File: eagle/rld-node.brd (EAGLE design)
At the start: 160 x 100 mm, 11 parts

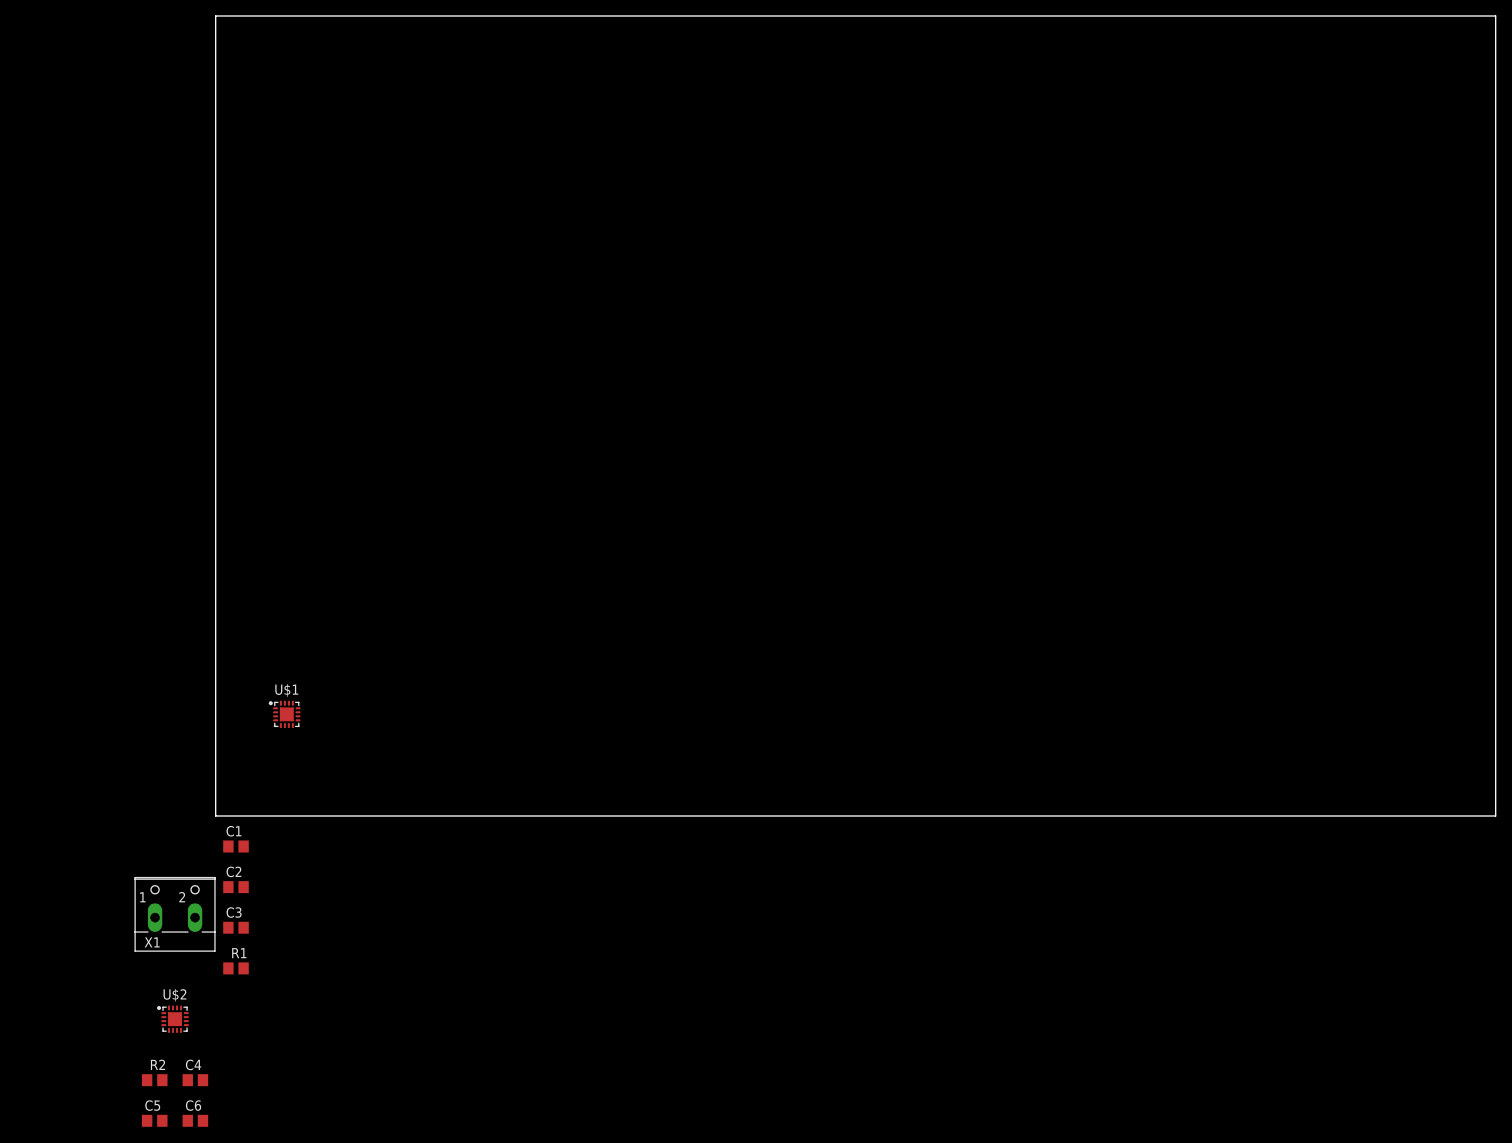
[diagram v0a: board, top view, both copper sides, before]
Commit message: Added synched layout
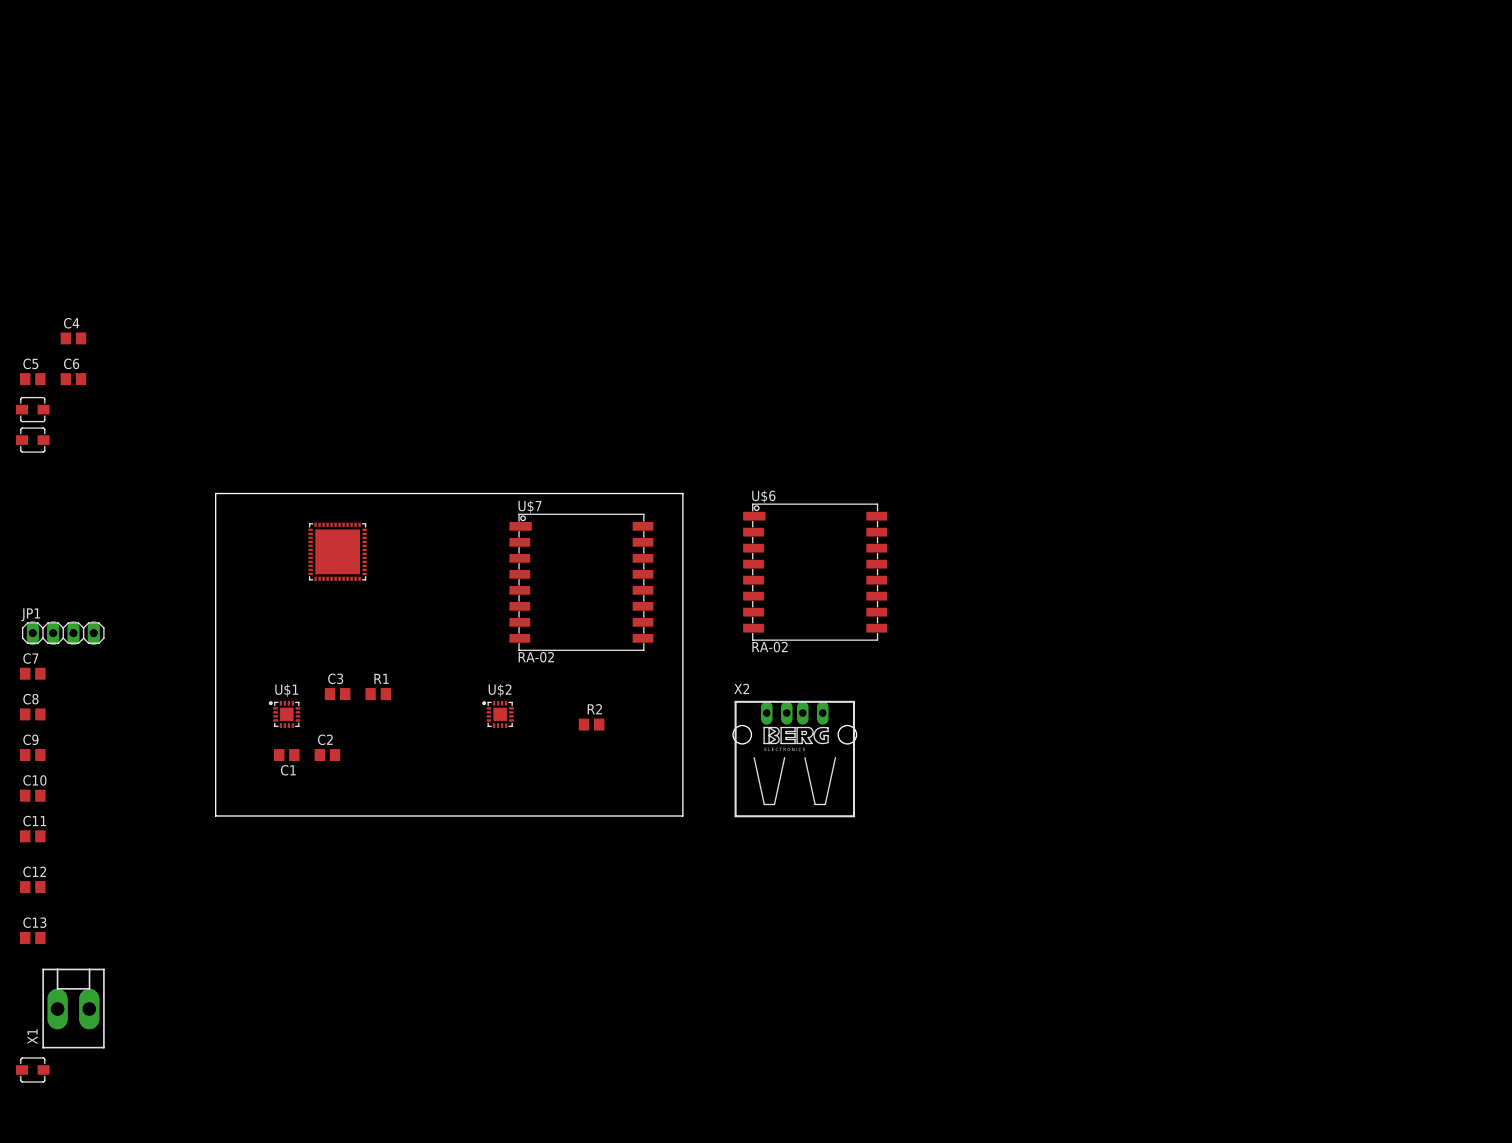
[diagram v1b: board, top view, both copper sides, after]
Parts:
- added C10, C7, C8: 100nF, rcl:C0805
- added C11: 4.7uF, rcl:C0805
- added C12: 10nF, rcl:C0805
- added C13: 1uF, rcl:C0805
- added C9: 4.7 uF, rcl:C0805
- added JP1: (no value), pinhead:1X04
- added U$3, U$4, U$8: IHLP-1212, inductor-vishay:1212BZ
- added U$5: STM32-F042X4/6-48, st-microelectronics:UFQFPN48-7X7
- added U$6, U$7: RA-02, ai-thinker:RA-01/RA-02
- added X2: (no value), con-berg:PN87520
- X1: device con-wago-500:W237-102 -> con-molex:KK-156-2
- moved C4 94.0 mm to (-17.8, 59.7)
- moved C5 94.0 mm to (-22.9, 54.6)
- moved C6 94.0 mm to (-17.8, 54.6)
- moved R2 70.4 mm to (47.0, 11.4)
- moved U$2 55.7 mm to (35.6, 12.7)
- moved R1 38.6 mm to (20.3, 15.2)
- moved C3 31.9 mm to (15.2, 15.2)
- moved C2 20.1 mm to (14.0, 7.62)
- moved X1 18.0 mm to (-17.8, -24.1)
- moved C1 13.1 mm to (8.89, 7.62), turned to 180 degrees
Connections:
- new net N$5: U$1.1, U$1.2, U$1.3, U$3.1
- new net N$6: U$2.1, U$2.2, U$2.3, U$4.1
- new net SPI1_MISO: U$5.16
- new net SPI1_MOSI: U$5.17
- new net SPI1_SCK: U$5.15
- new net SPI2_MISO: U$5.27
- new net SPI2_MOSI: U$5.28
- new net SPI2_SCK: U$5.21
- new net SWCLK: JP1.3, U$5.37
- new net SWDIO: JP1.2, U$5.34
- new net USB_D+: U$5.33
- new net USB_D-: U$5.32
- net +3V3: now also C10.2, C11.2, C12.2, C13.2, C7.2, C8.2, C9.2, JP1.4, U$4.2, U$5.24, U$5.48, U$5.9
- net +5V: now also U$3.2, X2.1
- net GND: now also C10.1, C11.1, C12.1, C13.1, C7.1, C8.1, C9.1, JP1.1, U$5.23, U$5.35, U$5.47, U$5.49, U$5.8, X1.1, X2.4; no longer X1.2
- net VCC: now also X1.2; no longer X1.1
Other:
- board size 160 x 100 mm -> 58.4 x 40.3 mm

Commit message: Nearly finished design
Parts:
- removed U$8: IHLP-1212, inductor-vishay:1212BZ
- removed X2: (no value), con-berg:PN87520
- added C14, C15: (no value), rcl:C0805
- added C16, C17: 22 µF, Eagle_WCAP-ASLI_rev20a:WCAP-ASLI_4X5.5(DXL)
- added JP2: (no value), pinhead:1X02
- added X3: (no value), con-wago-500:W237-102
- X1: device con-molex:KK-156-2 -> con-wago-500:W237-102
- moved C5 82.7 mm to (46.6, 9.70), turned to 270 degrees
- moved C4 82.3 mm to (42.6, 3.70), turned to 180 degrees
- moved X1 81.6 mm to (44.5, 28.6), turned to 90 degrees
- moved U$4 74.4 mm to (42.6, 11.7)
- moved C6 72.1 mm to (38.6, 9.70), turned to 90 degrees
- moved U$3 65.4 mm to (29.6, 11.7)
- moved U$6 63.9 mm to (11.0, 29.5)
- moved C13 51.0 mm to (13.5, 20.5), flipped to the bottom
- moved C10 49.4 mm to (18.5, 29.5), flipped to the bottom, turned to 270 degrees
- moved C9 45.1 mm to (18.5, 25.5), flipped to the bottom, turned to 270 degrees
- moved C12 43.7 mm to (9.50, 20.5), flipped to the bottom
- moved C7 40.0 mm to (13.5, 34.5), flipped to the bottom, turned to 180 degrees
- moved C11 39.2 mm to (4.50, 25.5), flipped to the bottom, turned to 270 degrees
- moved C8 39.0 mm to (9.50, 34.5), flipped to the bottom
- moved JP1 27.5 mm to (3.30, 6.80), turned to 90 degrees
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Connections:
- removed net SPI1_MISO: U$5.16
- removed net SPI1_MOSI: U$5.17
- removed net SPI1_SCK: U$5.15
- removed net SPI2_MISO: U$5.27
- removed net SPI2_MOSI: U$5.28
- removed net SPI2_SCK: U$5.21
- new net LORA1_D0: U$5.13, U$6.5
- new net LORA1_MISO: U$5.16, U$6.13
- new net LORA1_MOSI: U$5.17, U$6.14
- new net LORA1_NSS: U$5.14, U$6.15
- new net LORA1_RST: U$5.12, U$6.4
- new net LORA1_SCK: U$5.15, U$6.12
- new net LORA2_D0: U$5.25, U$7.5
- new net LORA2_MISO: U$5.27, U$7.13
- new net LORA2_MOSI: U$5.28, U$7.14
- new net LORA2_NSS: U$5.26, U$7.15
- new net LORA2_RST: U$5.22, U$7.4
- new net LORA2_SCK: U$5.21, U$7.12
- new net USART1_RX: JP2.1, U$5.31
- new net USART1_TX: JP2.2, U$5.30
- net +3V3: now also C14.2, C15.2, C16.1, C17.1, U$6.3, U$7.3
- net +5V: now also X3.1; no longer X2.1
- net GND: now also C14.1, C15.1, C16.2, C17.2, U$6.1, U$6.16, U$6.2, U$6.9, U$7.1, U$7.16, U$7.2, U$7.9, X1.2, X3.2; no longer X1.1, X2.4
- net VCC: now also X1.1; no longer X1.2
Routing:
- net GND: track 0.00 -> 273.7 mm, vias 0 -> 9
- net +3V3: track 0.00 -> 162.2 mm, vias 0 -> 4
- net LORA2_NSS: track 0.00 -> 68.5 mm, vias 0 -> 1
- net VCC: track 0.00 -> 63.9 mm
- net USART1_TX: track 0.00 -> 61.2 mm, vias 0 -> 1
- net USART1_RX: track 0.00 -> 57.0 mm, vias 0 -> 1
- net LORA2_MISO: track 0.00 -> 42.0 mm, vias 0 -> 1
- net LORA2_MOSI: track 0.00 -> 39.6 mm, vias 0 -> 1
- net LORA2_SCK: track 0.00 -> 35.6 mm, vias 0 -> 1
- net SWCLK: track 0.00 -> 32.5 mm
- net SWDIO: track 0.00 -> 29.2 mm
- net +5V: track 0.00 -> 29.2 mm
- net LORA1_D0: track 0.00 -> 28.9 mm, vias 0 -> 1
- net LORA2_D0: track 0.00 -> 27.3 mm, vias 0 -> 1
- net LORA1_NSS: track 0.00 -> 26.7 mm, vias 0 -> 1
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- added copper zone on layer 1, net GND
- added copper zone on layer 16, net GND
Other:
- board size 58.4 x 40.3 mm -> 50 x 40 mm
- board text added: "LORA1"
- board text added: "LORA2"
- board text added: "RPI"

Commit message: WIP
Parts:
- removed C15: (no value), rcl:C0805
- removed C17: 22 µF, Eagle_WCAP-ASLI_rev20a:WCAP-ASLI_4X5.5(DXL)
- removed JP1: (no value), pinhead:1X04
- removed U$1, U$2: TPS6214X, texas-instruments:VQFN16-3X3
- removed X3: (no value), con-wago-500:W237-102
- added H1, H2: MOUNT-PAD-ROUND2.8, holes:2,8-PAD
- added L1, L2: TPS6214X, texas-instruments:VQFN16-3X3
- added SYS: (no value), pinhead:1X04
- added X2: (no value), con-yamaichi:USB-A003
- moved C2 6.51 mm to (33.9, 16.2)
- moved C3 6.51 mm to (25.9, 16.2)
- moved C5 6.51 mm to (46.9, 16.2)
- moved C6 6.51 mm to (38.9, 16.2)
- moved U$3 6.51 mm to (29.9, 18.2)
- moved U$4 6.51 mm to (42.9, 18.2)
- moved C1 6.51 mm to (29.9, 10.2)
- moved C4 6.51 mm to (42.9, 10.2)
- moved R1 6.51 mm to (25.9, 11.2)
- moved R2 6.51 mm to (38.9, 11.2)
- moved C14 3.00 mm to (14.0, 18.0), turned to 180 degrees
- moved C16 3.00 mm to (20.0, 18.0)
- moved JP2 0.22 mm to (42.8, 36.4), turned to 90 degrees
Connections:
- net +3V3: now also L2.14, SYS.4; no longer C15.2, C17.1, JP1.4, U$2.14
- net +5V: now also L1.14, X2.1; no longer U$1.14, X3.1
- net GND: now also H1.B2,8, H2.B2,8, L1.15, L1.16, L1.17, L1.5, L1.6, L1.7, L1.8, L2.15, L2.16, L2.17, L2.5, L2.6, L2.7, L2.8, SYS.1, X2.4; no longer C15.1, C17.2, JP1.1, U$1.15, U$1.16, U$1.17, U$1.5, U$1.6, U$1.7, U$1.8, U$2.15, U$2.16, U$2.17, U$2.5, U$2.6, U$2.7, U$2.8, X3.2
- net N$1: now also L1.9; no longer U$1.9
- net N$2: now also L2.9; no longer U$2.9
- net N$3: now also L2.4; no longer U$2.4
- net N$4: now also L1.4; no longer U$1.4
- net N$5: now also L1.1, L1.2, L1.3; no longer U$1.1, U$1.2, U$1.3
- net N$6: now also L2.1, L2.2, L2.3; no longer U$2.1, U$2.2, U$2.3
- net SWCLK: now also SYS.3; no longer JP1.3
- net SWDIO: now also SYS.2; no longer JP1.2
- net VCC: now also L1.10, L1.11, L1.12, L1.13, L2.10, L2.11, L2.12, L2.13; no longer U$1.10, U$1.11, U$1.12, U$1.13, U$2.10, U$2.11, U$2.12, U$2.13
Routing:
- net GND: track 273.7 -> 291.0 mm, vias 9 -> 5
- net +3V3: track 162.2 -> 145.7 mm, vias 4 -> 3
- net VCC: track 63.9 -> 57.5 mm
- net LORA2_NSS: track 68.5 -> 74.0 mm
- net LORA1_D0: track 28.9 -> 24.3 mm
- net USART1_TX: track 61.2 -> 57.4 mm
- net +5V: track 29.2 -> 25.6 mm, vias 0 -> 1
- net SWCLK: track 32.5 -> 29.5 mm
- net SWDIO: track 29.2 -> 32.0 mm
- net LORA2_D0: track 27.3 -> 26.3 mm
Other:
- board text added: "* Only to be used by humans *"
- board text added: "+3V3"
- board text added: "12V"
- board text added: "C16"
- board text added: "GND"
- board text added: "RX"
- board text added: "SWCLK"
- board text added: "SWDIO"
- board text added: "TX"
